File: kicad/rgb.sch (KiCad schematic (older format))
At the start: 25 parts, among them J1 1935776, J2 102-6164-ND, J3 102-6164-ND, J4 Conn_01x04, J5 Conn_01x02, Q1 DMG9926USD, Q2 DMG9926USD, Q3 DMG9926USD, Q4 DMG9926USD, SW1 450-1642-ND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

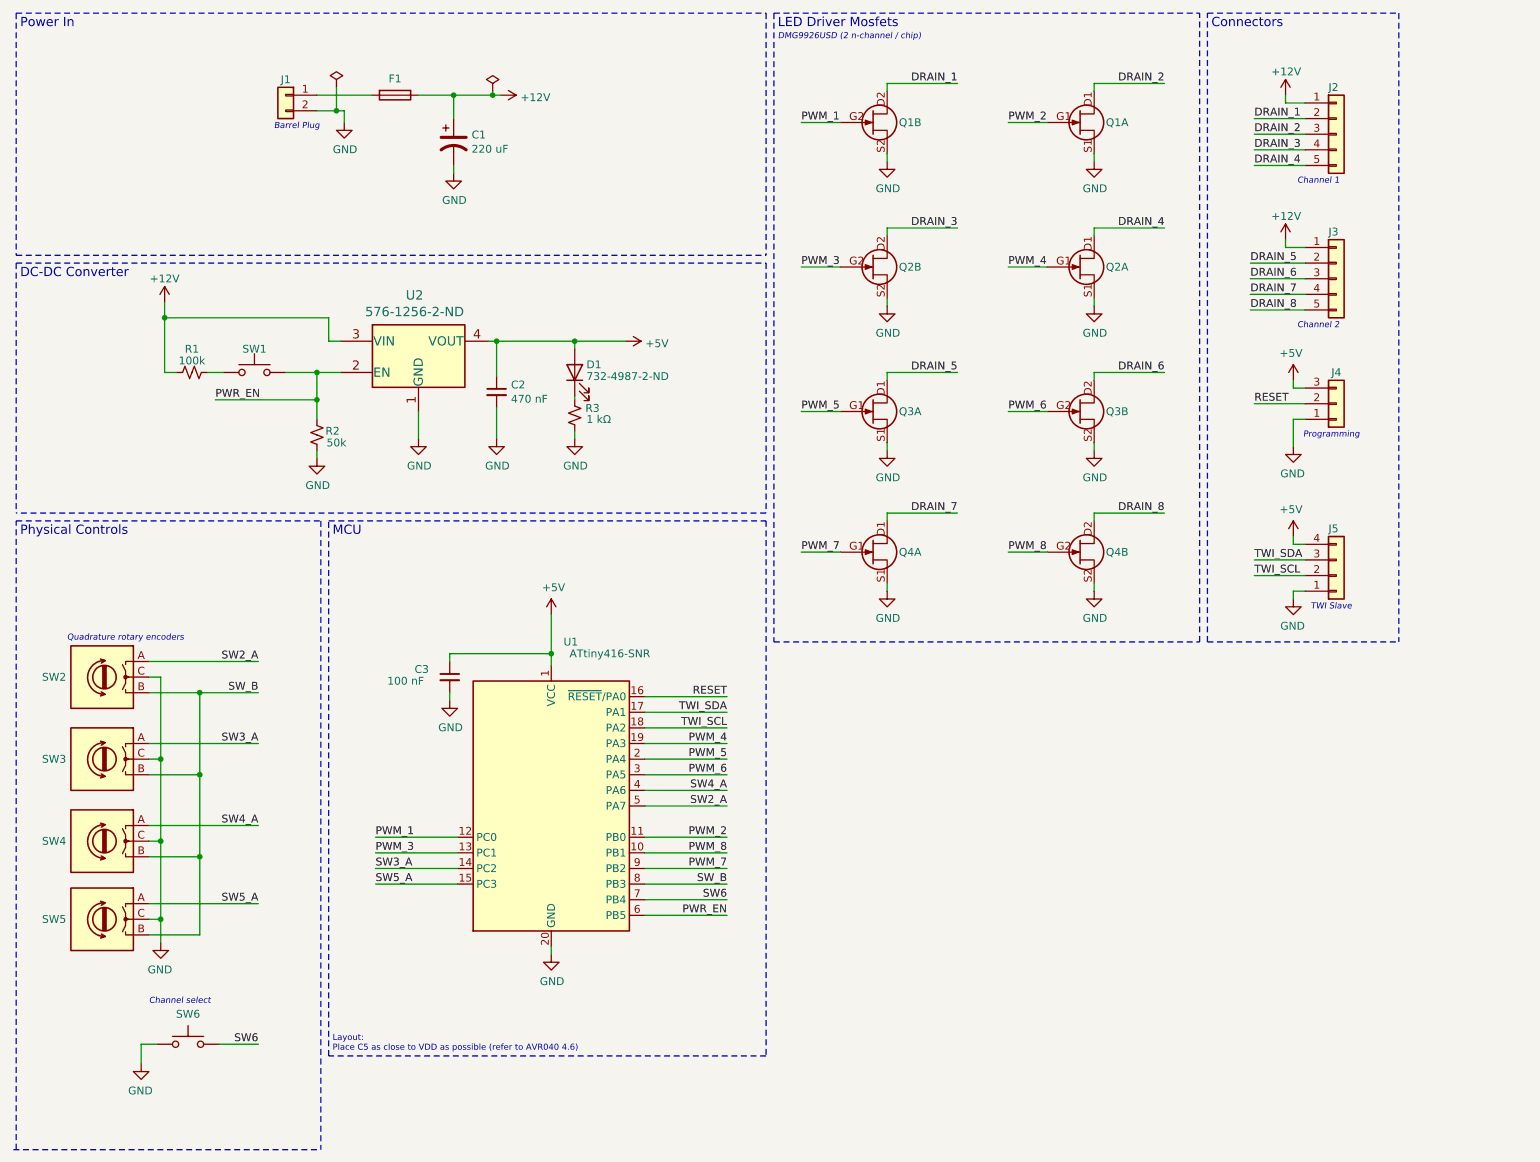
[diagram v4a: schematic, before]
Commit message: changed vin connector, touchups
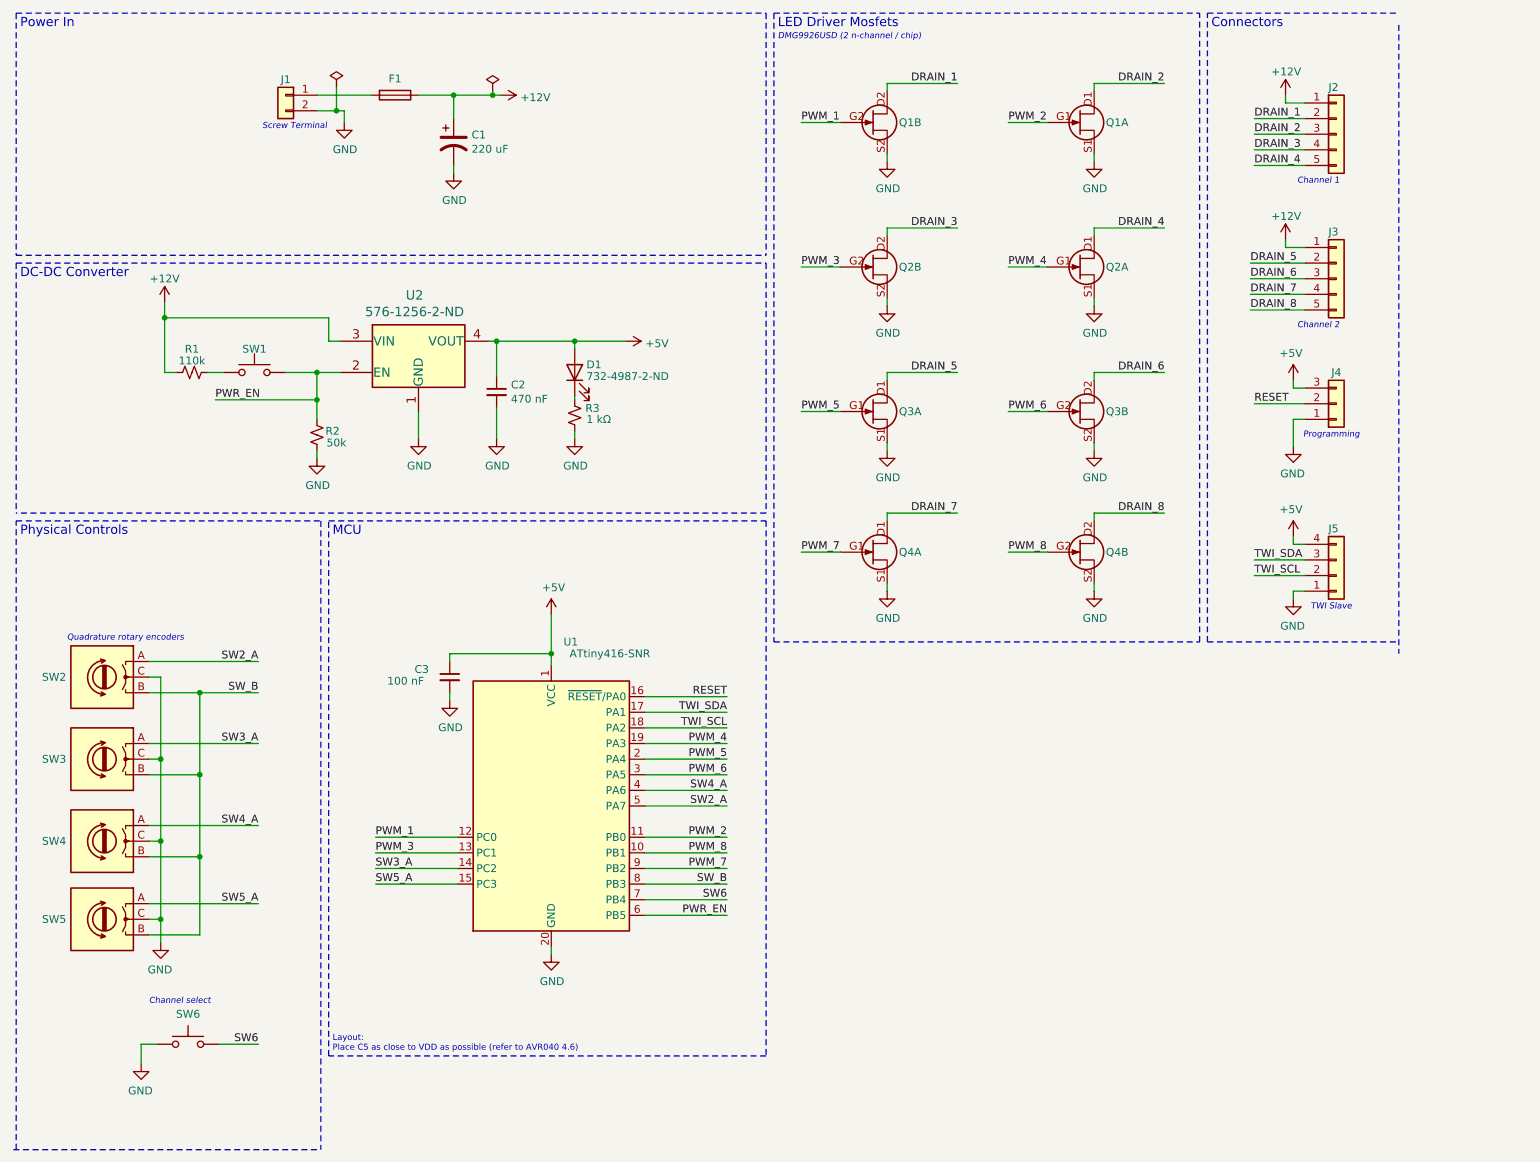
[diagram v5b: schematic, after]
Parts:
- J1: footprint rgb_footprints:barrel jack -> rgb_footprints:CUI_TB001-500-02BE
- R1: value 100k -> 110k; footprint Resistor_SMD:R_0603_1608Metric_Pad1.05x0.95mm_HandSolder -> Resistor_SMD:R_0805_2012Metric_Pad1.20x1.40mm_HandSolder
- R2: footprint Resistor_SMD:R_0603_1608Metric_Pad1.05x0.95mm_HandSolder -> Resistor_SMD:R_0805_2012Metric_Pad1.20x1.40mm_HandSolder
- R3: footprint Resistor_SMD:R_0603_1608Metric_Pad0.98x0.95mm_HandSolder -> Resistor_SMD:R_0805_2012Metric_Pad1.20x1.40mm_HandSolder
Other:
- note added: "Screw Terminal\n"
- note removed: "Barrel Plug"

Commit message: layout done
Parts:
- added R1: 0.005, Resistor_SMD:R_1020_2550Metric_Pad1.33x5.20mm_HandSolder, symbol Device:R_US
- added R2: 10k, Resistor_SMD:R_0805_2012Metric_Pad1.20x1.40mm_HandSolder, symbol Device:R_Small_US
- added U1: ZXCT1109, Package_TO_SOT_SMD:SOT-23, symbol Amplifier_Current:ZXCT1107
- C1: value 220 uF -> 3300 uF; footprint Capacitor_SMD:CP_Elec_6.3x7.7 -> Capacitor_THT:CP_Radial_D12.5mm_P5.00mm
- R4: renamed from R2; value 50k -> 50 kΩ
- U2: value 576-1256-2-ND -> MIC5203-5.0
- renumbered C2 to C3, C3 to C4, R1 to R3, R3 to R5, U1 to U3
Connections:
- net +12V: now also R1.2, U1.2 (Vs-); no longer F1.1
- net GND: now also R2.2
- net SW6: now also U3.8 (PB3); no longer U3.7 (PB4)
- net SW2_A renamed SW_A1
- net SW_A1: now also SW3.A, U3.4 (PA6); no longer U3.5 (PA7)
- net SW3_A renamed SW_B1
- net SW_B1: now also SW2.B, SW4.B; no longer SW3.A
- net SW4_A renamed SW_A2
- net SW_A2: now also SW5.A, U3.5 (PA7); no longer U3.4 (PA6)
- net SW5_A renamed SW_B2
- net SW_B2: now also SW3.B, SW5.B; no longer SW5.A
- removed net SW_B: SW2.B, SW3.B, SW4.B, SW5.B, U3.8 (PB3)
- new net: F1.1, R1.1, U1.1 (Vs+)
- new net SENSE: R2.1, U1.3 (OUT), U3.7 (PB4)
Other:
- moved on the sheet: C3, C4, D1, F1, J1, R3, R4, R5, SW1, SW2, SW3, SW4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

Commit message: rev0
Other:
- moved on the sheet: C3, C4, D1, J2, J3, J4, J5, Q1A, Q1B, Q2A, Q2B, Q3A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

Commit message: minor changes
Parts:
- U2: symbol MIC5203:MIC5203-5.0YM4-TR -> rgb-rescue:MIC5203-5.0YM4-TR-MIC5203
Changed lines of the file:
@@
 $EndComp
 $Comp
-L MIC5203:MIC5203-5.0YM4-TR U2
+L rgb-rescue:MIC5203-5.0YM4-TR-MIC5203 U2
 U 1 1 5FEE6BDA
 P 7825 1250
